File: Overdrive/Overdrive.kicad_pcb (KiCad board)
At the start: 2 copper layers, 85 x 86 mm, 44 parts, among them J2 Barrel_Jack_Switch, J3 Stereo In, J4 Mono Out, Q1 2N2222, Q2 2N2222, SW1 Footswitch, U1 RC4558

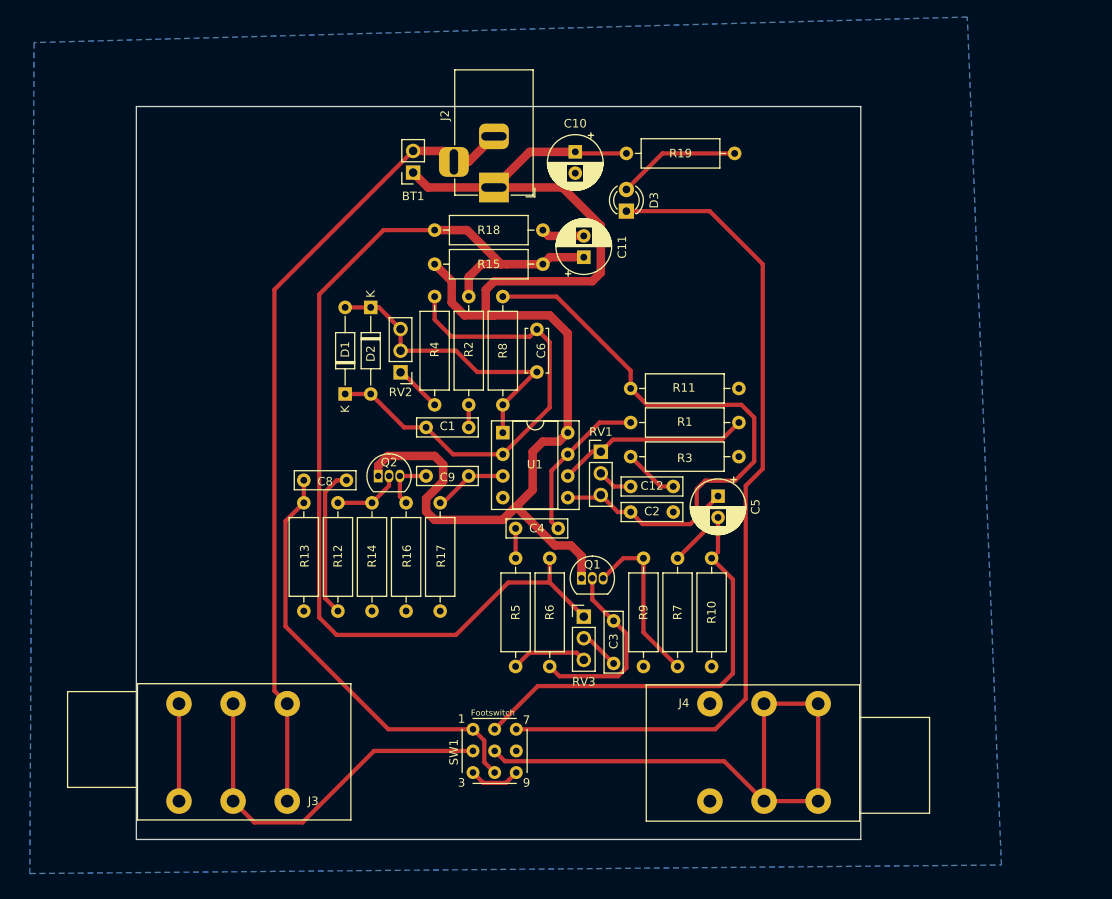
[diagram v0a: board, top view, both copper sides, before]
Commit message: Fixed PCB errors and added logos
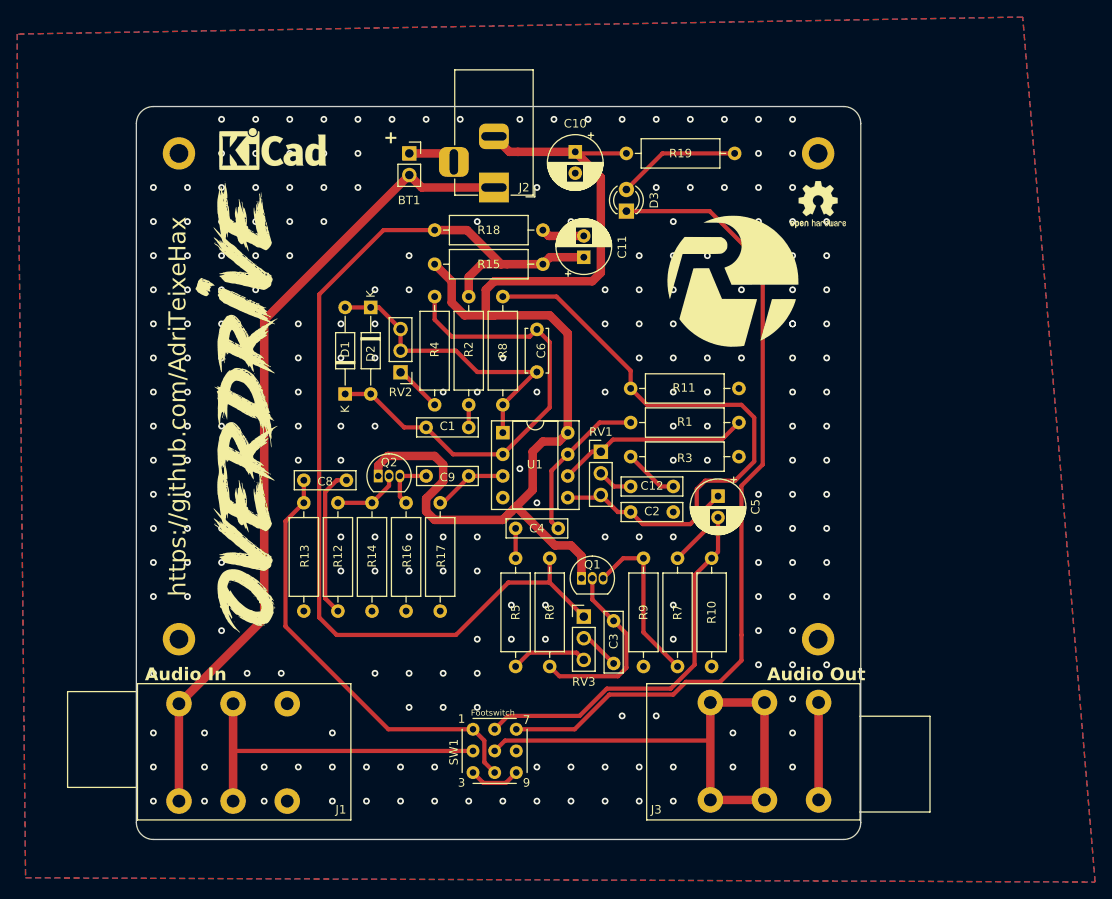
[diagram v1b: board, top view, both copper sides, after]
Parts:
- added G***: LOGO, LOGO, F.Cu at (159.0, 88.0)
- added G***: LOGO, LOGO, F.Cu at (104.0, 103.0)
- added G***: LOGO, LOGO, B.Cu at (98.8, 102.2)
- added J1: Stereo In, Connector_Audio:Jack_6.35mm_Neutrik_NRJ6HM-1-AU_Horizontal, F.Cu at (106.7, 149.0)
- added J5: M2, MountingHole:MountingHole_2.2mm_M2_DIN965_Pad, F.Cu at (169.0, 73.0)
- added J6: M2, MountingHole:MountingHole_2.2mm_M2_DIN965_Pad, F.Cu at (94.0, 130.0)
- added J7: M2, MountingHole:MountingHole_2.2mm_M2_DIN965_Pad, F.Cu at (169.0, 130.0)
- added REF**: OSHW-Logo2_7.3x6mm_SilkScreen, Symbol:OSHW-Logo2_7.3x6mm_SilkScreen, F.Cu at (169.0, 79.0)
- added REF**: KiCad-Logo_5mm_SilkScreen, Symbol:KiCad-Logo_5mm_SilkScreen, F.Cu at (105.0, 73.0)
- J3: value Stereo In -> Mono Out
- J4: value Mono Out -> M2; footprint Connector_Audio:Jack_6.35mm_Neutrik_NRJ6HM-1-AU_Horizontal -> MountingHole:MountingHole_2.2mm_M2_DIN965_Pad
- moved J4 89.7 mm to (94.0, 73.0)
- moved J3 51.0 mm to (156.3, 137.4), turned to 0 degrees
- moved BT1 2.29 mm to (121.0, 73.0), turned to 0 degrees
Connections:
- BT1 pad 1: +9V -> Net-(BT1-+)
- J2 pad 1: +9V -> Net-(BT1--)
- J2 pad 2: Net-(BT1--) -> +9V
- J2 pad 3: Net-(BT1--) -> Net-(BT1-+)
- J3 pad T: Net-(BT1--) -> Net-(J3-PadR)
- J3 pad TN: Net-(BT1--) -> Net-(J3-PadR)
- SW1 pad 2: Net-(J3-PadR) -> Net-(J1-PadR)
- SW1 pad 5: Net-(J4-PadR) -> Net-(J3-PadR)
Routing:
- net Net-(J4-PadR): track 69.6 -> 0.00 mm
- net Net-(J1-PadR): track 0.00 -> 45.1 mm
- net Net-(J3-PadR): track 44.1 -> 68.3 mm
- net +9V: track 152.7 -> 137.1 mm
- net Net-(BT1-+): track 0.00 -> 5.65 mm
- net Net-(C5-Pad2): track 50.3 -> 45.0 mm
- net Net-(D3-K): track 98.8 -> 95.9 mm
- net GND: vias 0 -> 231
- added copper zone on F.Cu, net GND
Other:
- outline, holes or cut-outs redrawn
- board text added: "+"
- board text added: "Audio In"
- board text added: "Audio Out"
- board text added: "https://github.com/AdriTeixeHax"
